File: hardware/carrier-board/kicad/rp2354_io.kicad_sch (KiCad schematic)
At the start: 7 parts, among them J12 USB-C prog, J13 SWD, SW1 USB sel, U5 RP2354B, U6 USBLC6-2, Y1 12MHz

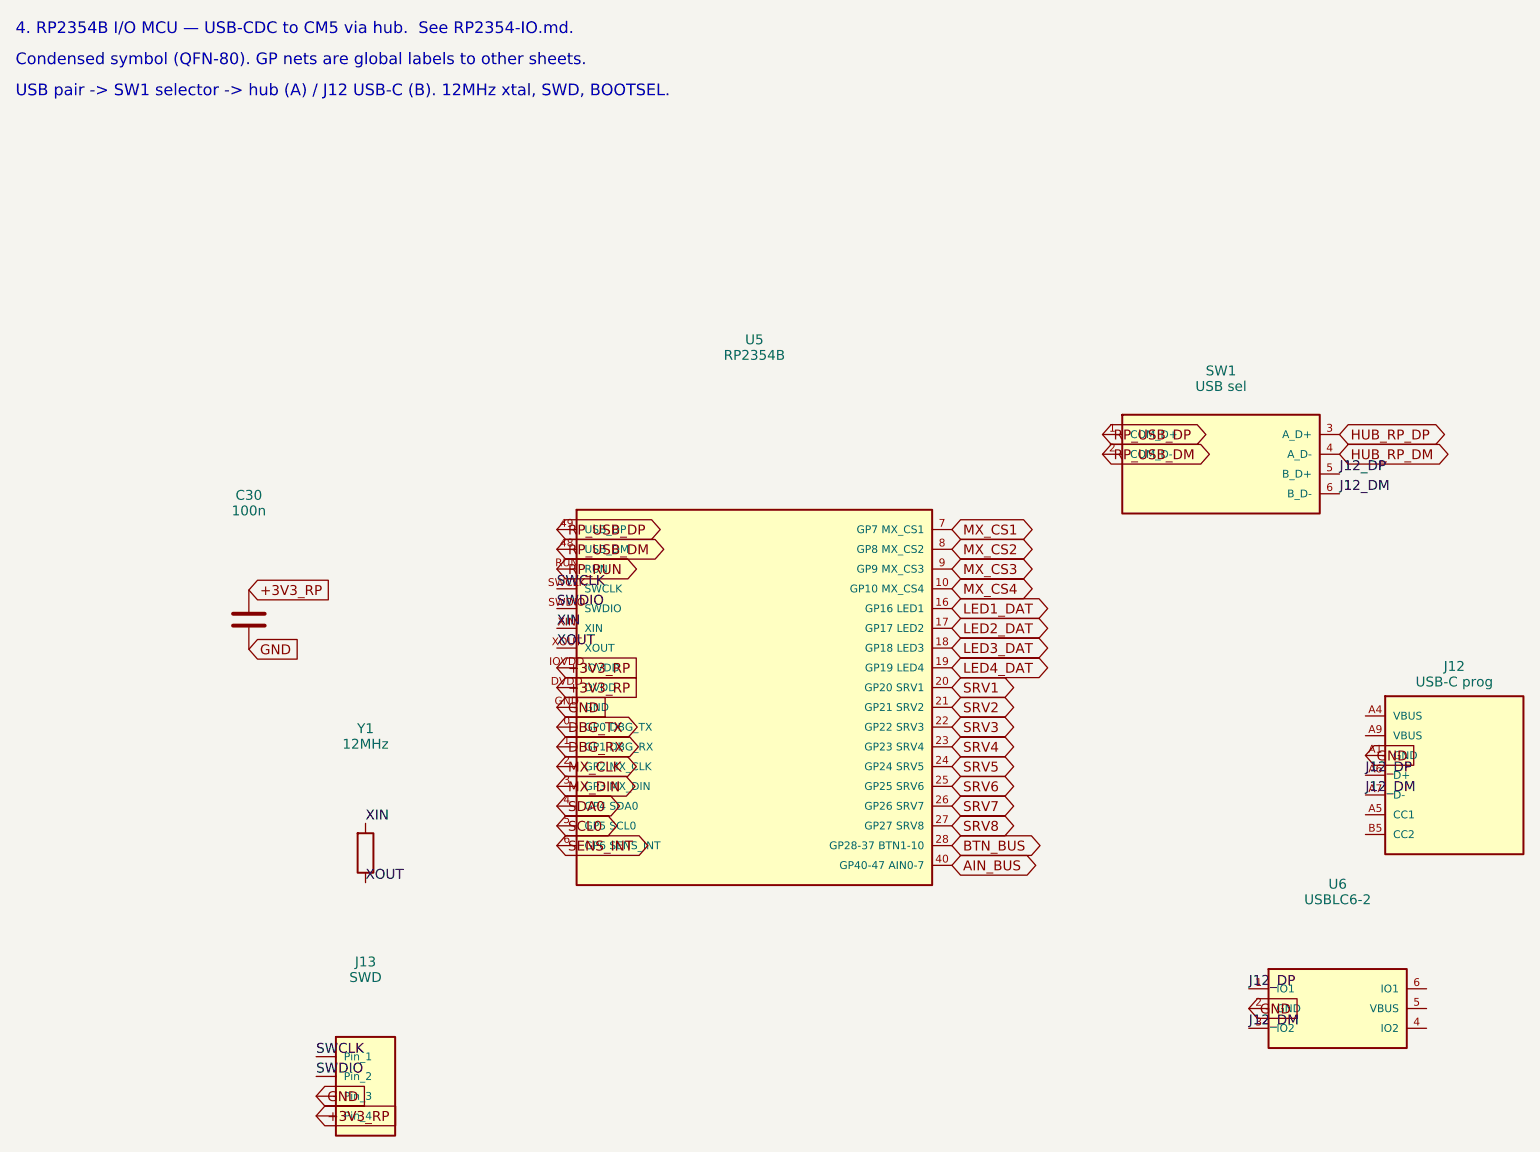
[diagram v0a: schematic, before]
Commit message: hardware(carrier): replace USB 2.0 hub with VL817 USB 3.1 4-port hub
Swap the on-board USB2514B (USB 2.0) for a VIA VL817 4-port USB 3.1 Gen1
(5 Gbps) hub with four USB-C downstream receptacles (J40-J43), upstream on
a CM5 USB 3.0 port. The CM5 exposes 2x USB 3.0 + 1x USB 2.0, so:

  - USB3 #0 -> VL817 upstream (SuperSpeed + USB 2.0)
  - USB3 #1 -> RP2354B CDC (now OFF-hub, via SW1) -> frees all 4 hub ports
  - USB2    -> backpack phone uplink (J11)

Generator (populate_sheets.py):
  - new VL817 condensed symbol (USB2 + SS per port, xtal, reset, straps)
  - new USB-C 3.1 receptacle symbol (VBUS/GND/CC/D+-/one SS lane)
  - CM5 symbol gains USB3 SuperSpeed pins + 2nd/3rd USB ports
  - rewrite sh_usb(): per-port CC Rp pull-ups (56k, host/DFP), VBUS PTC off
    +5V, USBLC6 ESD, SS AC-coupling caps at each TX, 25 MHz hub clock
  - SW1 'A' side rerouted from hub to the dedicated CM5 USB port

Docs: CONNECTORS, POWER, BOM, REQUIREMENTS, BLOCK-DIAGRAM, READMEs updated
for the USB 3.1 hub, USB-C downstream ports, and off-hub RP2354B link.

All 11 sheets regenerated; S-expressions balanced and cross-sheet global
nets verified consistent.

Co-Authored-By: Claude Opus 4.8 <noreply@anthropic.com>
Claude-Session: https://claude.ai/code/session_01DgiE5SHRCeyk1gvfvshMGa
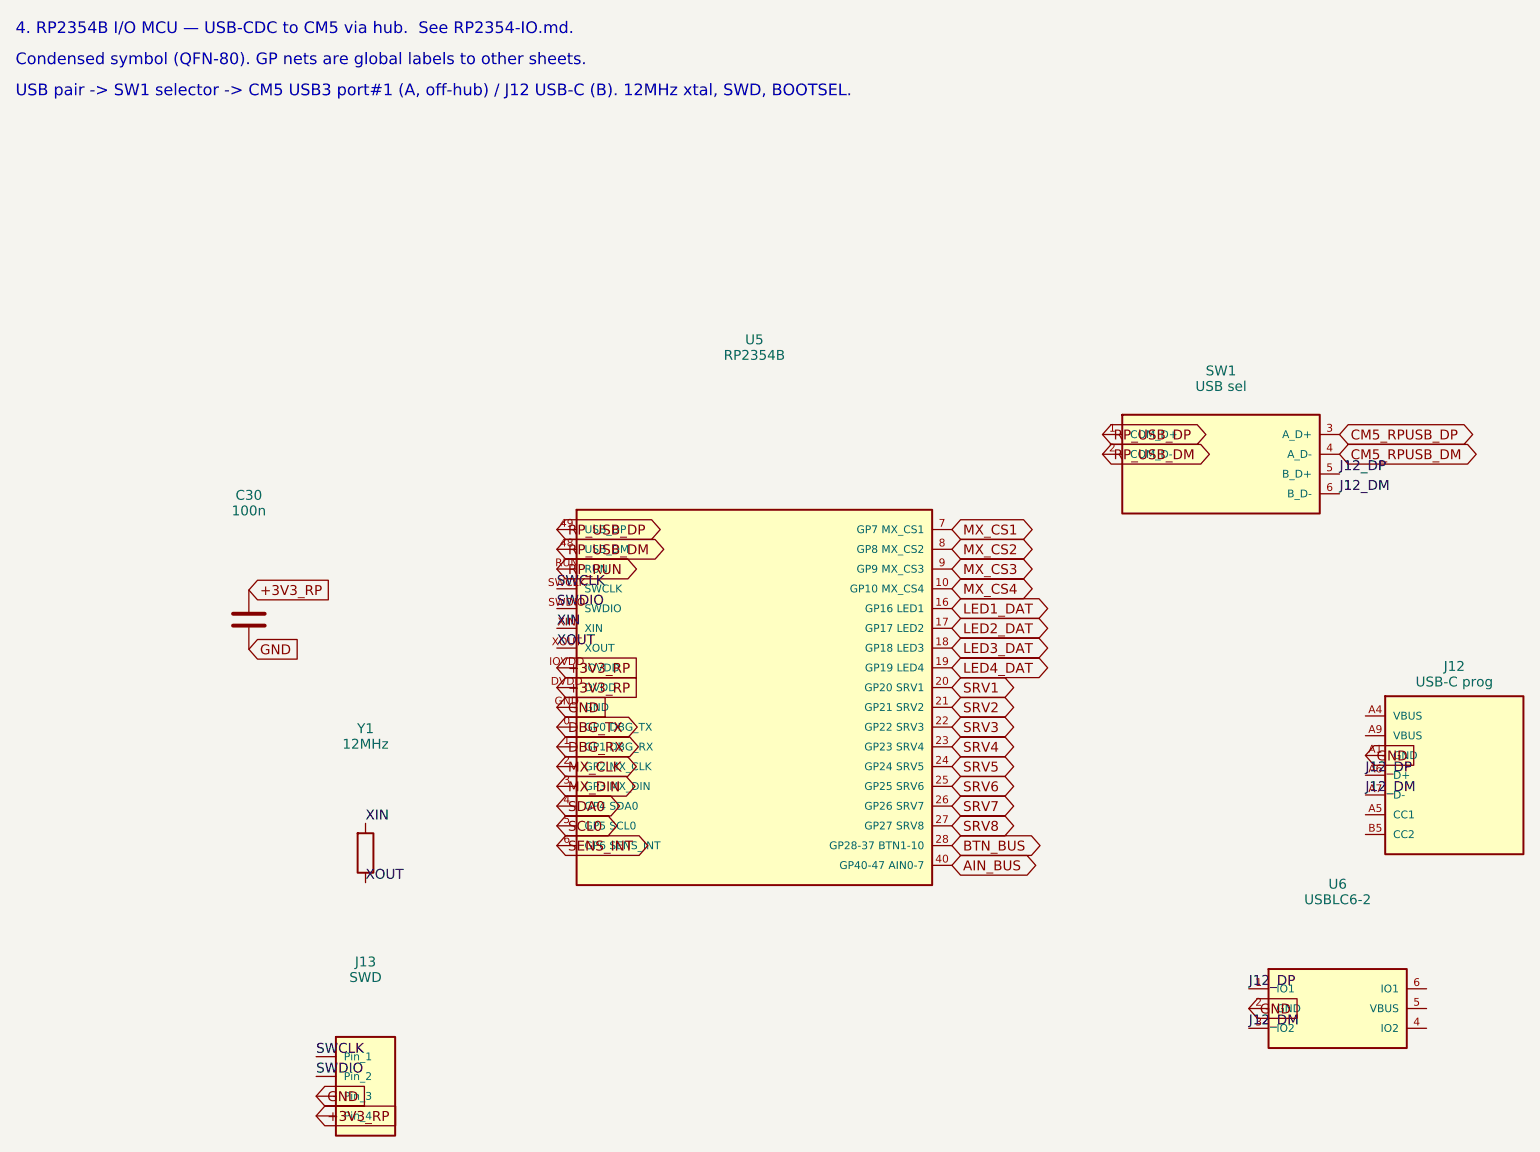
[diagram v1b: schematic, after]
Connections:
- net HUB_RP_DM renamed CM5_RPUSB_DM
- net HUB_RP_DP renamed CM5_RPUSB_DP
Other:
- note added: "USB pair -> SW1 selector -> CM5 USB3 port#1 (A, off-hub) / J12 USB-C (B). 12MHz xtal, SWD, BOOTSEL."
- note removed: "USB pair -> SW1 selector -> hub (A) / J12 USB-C (B). 12MHz xtal, SWD, BOOTSEL."
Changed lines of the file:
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@@
   (text "4. RP2354B I/O MCU — USB-CDC to CM5 via hub.  See RP2354-IO.md." (at 15 15.0 0) (effects (font (size 1.5 1.5)) (justify left bottom)))
   (text "Condensed symbol (QFN-80). GP nets are global labels to other sheets." (at 15 19.0 0) (effects (font (size 1.5 1.5)) (justify left bottom)))
-  (text "USB pair -> SW1 selector -> hub (A) / J12 USB-C (B). 12MHz xtal, SWD, BOOTSEL." (at 15 23.0 0) (effects (font (size 1.5 1.5)) (justify left bottom)))
+  (text "USB pair -> SW1 selector -> CM5 USB3 port#1 (A, off-hub) / J12 USB-C (B). 12MHz xtal, SWD, BOOTSEL." (at 15 23.0 0) (effects (font (size 1.5 1.5)) (justify left bottom)))
   (symbol
     (lib_id "MCU_RaspberryPi:RP2354B")
@@
   (global_label "RP_USB_DP" (shape bidirectional) (at 154.76 66.19 180) (effects (font (size 1.27 1.27)) (justify left)))
   (global_label "RP_USB_DM" (shape bidirectional) (at 154.76 68.73 180) (effects (font (size 1.27 1.27)) (justify left)))
-  (global_label "HUB_RP_DP" (shape bidirectional) (at 185.24 66.19 0) (effects (font (size 1.27 1.27)) (justify left)))
-  (global_label "HUB_RP_DM" (shape bidirectional) (at 185.24 68.73 0) (effects (font (size 1.27 1.27)) (justify left)))
+  (global_label "CM5_RPUSB_DP" (shape bidirectional) (at 185.24 66.19 0) (effects (font (size 1.27 1.27)) (justify left)))
+  (global_label "CM5_RPUSB_DM" (shape bidirectional) (at 185.24 68.73 0) (effects (font (size 1.27 1.27)) (justify left)))
   (label "J12_DP" (at 185.24 71.27 0) (effects (font (size 1.27 1.27)) (justify left bottom)))
   (label "J12_DM" (at 185.24 73.81 0) (effects (font (size 1.27 1.27)) (justify left bottom)))
